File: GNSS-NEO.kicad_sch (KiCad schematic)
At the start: 28 parts, among them J3 Conn_Coaxial, J4 Conn_Coaxial_Small, SW1 SW_Push, SW2 SW_Push, U2 NEO-M9N

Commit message: next revision pcb progress
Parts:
- removed D7: BESDU0603-14, Diode_SMD:D_0603_1608Metric, symbol Device:D_TVS
- removed TP1: LNA_EN, TestPoint:TestPoint_Loop_D1.80mm_Drill1.0mm_Beaded, symbol Connector:TestPoint_Probe
- added C28: 100nF, Capacitor_SMD:C_0402_1005Metric, symbol Device:C_Small
- added C30: 10uF, Capacitor_SMD:C_0402_1005Metric, symbol Device:C_Small
- added C31: 47pF C0G/NP0, Capacitor_SMD:C_0402_1005Metric, symbol Device:C_Small
- added C32: 10uF, Capacitor_SMD:C_0603_1608Metric, symbol Device:C_Small
- added C33: 22pF C0G/NP0, Capacitor_SMD:C_0402_1005Metric, symbol Device:C_Small
- added C34, C35: 10nF, Capacitor_SMD:C_0402_1005Metric_Pad0.74x0.62mm_HandSolder, symbol Device:C_Small
- added D1: TI ESD501, Package_SON:Texas_DPY0002A_0.6x1mm_P0.65mm, symbol Device:D_TVS
- added D8: ESD501, Package_SON:Texas_DPY0002A_0.6x1mm_P0.65mm, symbol Device:D_TVS
- added FB2: BLM18HG601SN1D, Inductor_SMD:L_0603_1608Metric, symbol Device:FerriteBead
- added FL1: B39162B4327P810, Filter:Filter_1411-5_1.4x1.1mm, symbol Filter:SF14-1575F5UUC1
- added JP4: SolderJumper_3_Bridged12, Jumper:SolderJumper-3_P1.3mm_Bridged12_RoundedPad1.0x1.5mm_NumberLabels, symbol Jumper:SolderJumper_3_Bridged12
- added Q2: AO3401A, Package_TO_SOT_SMD:SOT-23, symbol Transistor_FET:AO3401A
- added Q5: BSS138, Package_TO_SOT_SMD:SOT-23, symbol Transistor_FET:BSS138
- added R30, R34: 100k, symbol Device:R_Small
- added R31: 1k, symbol Device:R_Small
- added R32: 0, Resistor_SMD:R_0402_1005Metric_Pad0.72x0.64mm_HandSolder, symbol Device:R
- added R33: 68, Resistor_SMD:R_0402_1005Metric_Pad0.72x0.64mm_HandSolder, symbol Device:R
- added R35, R36: 100, Resistor_SMD:R_0402_1005Metric_Pad0.72x0.64mm_HandSolder, symbol Device:R
- added U8: TPS259573DSGR, easyeda2kicad:WSON-8_L2.0-W2.0-P0.50-TL-EP, symbol easyeda2kicad:TPS259573DSGR
- C10: value 100nF -> 1uF XR7
- L1: value 22nH -> 47nH; LCSC Part C6364694 -> C98077
- R13: value 10 -> 68 ohm >=500mW; footprint Resistor_SMD:R_0402_1005Metric -> Resistor_SMD:R_1206_3216Metric_Pad1.30x1.75mm_HandSolder
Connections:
- net +3V3: now also C28.1
- net GND: now also C28.2, C30.2, C32.1, C33.2, C34.2, C35.2, D1.1 (A1), D8.2 (A2), FL1.2, FL1.3, FL1.5, Q5.2 (S), R34.2, R35.1, R36.1
- net GPS_ANT: now also R33.2, R35.2; no longer L1.1, R27.2, R28.2
- net VCC_RF: now also JP4.3 (B); no longer R13.2
- net LNA_EN: now reaches U2.14 (LNA_EN)
- net LNA_EN: now also R31.2
- net at C10.1, L1.2, R13.1: now also C33.1
- net AFT_GPS_ANT: no longer names the net of J3.1 (In), R28.1
- net AFT_GPS_ANT: now also D1.2 (A2)
- new net: C30.1, C32.2, FB2.1, Q2.2 (S), R30.1
- new net: C35.1, FL1.1, R32.2
- new net: FB2.2, JP4.2 (C)
- new net: C31.1, C34.1, R32.1
- new net: C31.2, D8.1 (A1), L1.1, R27.2, R28.2
- new net: FL1.4, R33.1, R36.2
- new net: Q5.1 (G), R31.1, R34.1
- new net: Q2.1 (G), Q5.3 (D), R30.2
- new net: Q2.3 (D), R13.2
- new net +5V: JP4.1 (A)
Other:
- note added: "Active Antenna only"
- note added: "Antenna only powered when module is not in sleep mode"
- note added: "Attenuate 10dB"
- note added: "Bandpass GNSS SAW filter"
- note added: "Current limiting"
- note added: "If using VCC_RF, drop to 10 ohms"
- note added: "Optional Matching"
- note added: "maybe: replace with TPS2553"
- moved on the sheet: C10, D2, D3, J3, J4, JP1, JP2, JP3, JP5, L1, R10, R11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

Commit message: update schematic with new eFuse and add journal.md
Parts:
- removed U8: TPS259573DSGR, easyeda2kicad:WSON-8_L2.0-W2.0-P0.50-TL-EP, symbol easyeda2kicad:TPS259573DSGR
- added BT3: Battery_Cell, symbol Device:Battery_Cell
- added C39: 10uF, Capacitor_SMD:C_0402_1005Metric, symbol Device:C_Small
- added C40: 2.2nF, symbol Device:C_Small
- added C41: 1uF, Capacitor_SMD:C_0402_1005Metric, symbol Device:C_Small
- added C42: 3.3nF, symbol Device:C_Small
- added JP7: DISABLE_PROT, symbol Jumper:SolderJumper_2_Open
- added R29: 200k, symbol Device:R_Small
- added R38, R39: 100k, symbol Device:R_Small
- added R41: 10k, symbol Device:R_Small
- added R42: 6.65k, symbol Device:R_Small
- added R43: 47k, symbol Device:R_Small
- added U5: TPS259470LRPWR, easyeda2kicad:VQFN-10_L2.0-W2.0-P0.45-TL, symbol easyeda2kicad:TPS259470LRPWR
- C28: value 100nF -> 10uF
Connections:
- net +3V3: now also C41.2, JP7.1 (A), R29.1, R39.1, R41.1, R43.1, U5.5 (IN); no longer C16.1, C17.1, C28.1, JP1.1 (A), R8.1, U2.22 (V_BCKP), U2.23 (VCC)
- net GND: now also BT3.2 (-), C39.2, C40.1, C41.1, C42.2, R38.2, R42.2, U5.8 (GND)
- new net: BT3.1 (+), U2.22 (V_BCKP)
- new net: R41.2, U5.1 (EN/UVLO)
- new net: C40.2, U5.10 (ITIMER)
- new net: R29.2, R38.1, U5.2 (OVLO/OVCSEL)
- new net: R43.2, U5.3 (PG/AUXOFF)
- new net: C42.1, U5.7 (DVDT)
- new net: R42.1, U5.9 (ILM)
- new net 3V3_GNSS: C16.1, C17.1, C28.1, C39.1, JP1.1 (A), JP7.2 (B), R8.1, U2.23 (VCC), U5.6 (OUT)
- new net FLT_GNSS: R39.2, U5.4 (~{FLT}/PGTH)
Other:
- moved on the sheet: R14, R7, SW1, SW2, TP2, U2

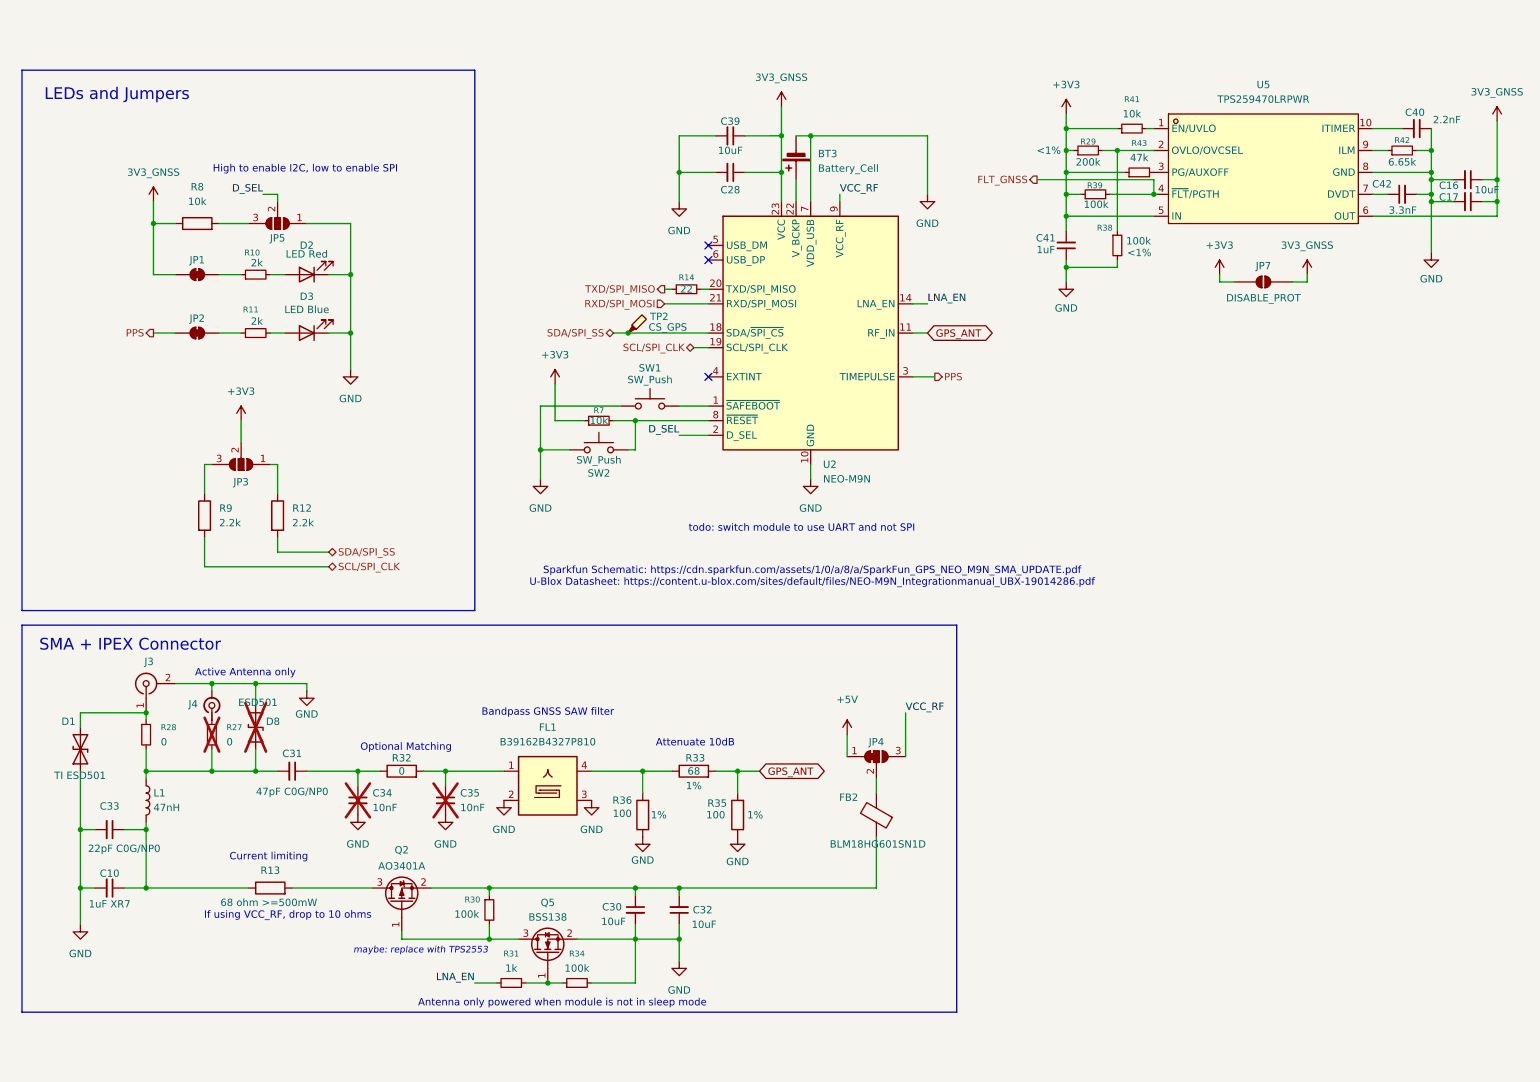
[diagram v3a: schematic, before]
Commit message: revise efuse, add bat
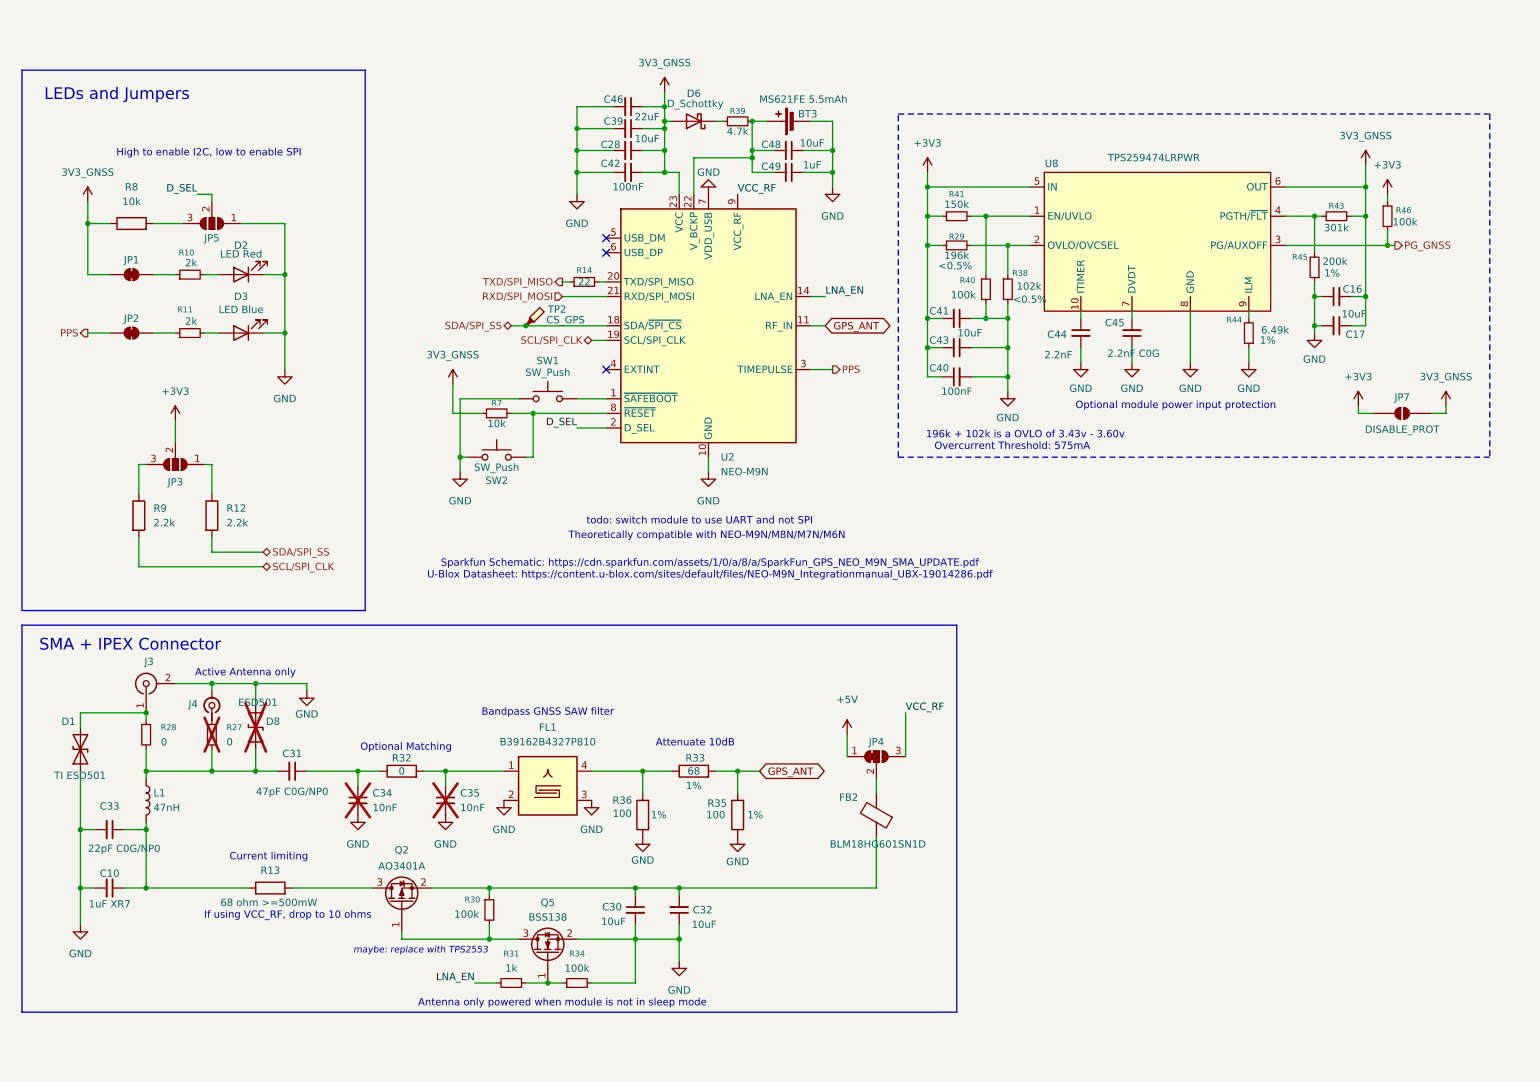
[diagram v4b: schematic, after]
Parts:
- removed R42: 6.65k, symbol Device:R_Small
- removed U5: TPS259470LRPWR, easyeda2kicad:VQFN-10_L2.0-W2.0-P0.45-TL, symbol easyeda2kicad:TPS259470LRPWR
- added C43, C48: 10uF, Capacitor_SMD:C_0402_1005Metric, symbol Device:C_Small
- added C44: 2.2nF, symbol Device:C_Small
- added C45: 2.2nF C0G, Capacitor_SMD:C_0402_1005Metric, symbol Device:C_Small
- added C46: 22uF, Capacitor_SMD:C_0805_2012Metric, symbol Device:C_Small
- added C49: 1uF, Capacitor_SMD:C_0402_1005Metric, symbol Device:C_Small
- added D6: D_Schottky, symbol Device:D_Schottky
- added R40, R46: 100k, symbol Device:R_Small
- added R44: 6.49k, Resistor_SMD:R_0603_1608Metric_Pad0.98x0.95mm_HandSolder, symbol Device:R_Small
- added R45: 200k, Resistor_SMD:R_0603_1608Metric_Pad0.98x0.95mm_HandSolder, symbol Device:R_Small
- added U8: TPS259474LRPWR, easyeda2kicad:VQFN-10_L2.0-W2.0-P0.45-TL, symbol easyeda2kicad:TPS259474LRPWR
- BT3: value Battery_Cell -> MS621FE 5.5mAh; footprint (none) -> Battery:BatteryHolder_Seiko_MS621F; now left out of the parts list
- C16, C39: footprint Capacitor_SMD:C_0402_1005Metric -> Capacitor_SMD:C_0603_1608Metric
- C40: value 2.2nF -> 100nF; footprint (none) -> Capacitor_SMD:C_0402_1005Metric
- C41: value 1uF -> 10uF; footprint Capacitor_SMD:C_0402_1005Metric -> Capacitor_SMD:C_0603_1608Metric
- C42: value 3.3nF -> 100nF; footprint (none) -> Capacitor_SMD:C_0402_1005Metric
- R29: value 200k -> 196k; footprint (none) -> Resistor_SMD:R_0603_1608Metric_Pad0.98x0.95mm_HandSolder; Tolerance <1% -> <0.5%
- R38: value 100k -> 102k; footprint (none) -> Resistor_SMD:R_0603_1608Metric_Pad0.98x0.95mm_HandSolder; Tolerance <1% -> <0.5%
- R39: value 100k -> 4.7k; footprint (none) -> Resistor_SMD:R_0402_1005Metric
- R41: value 10k -> 150k
- R43: value 47k -> 301k
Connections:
- net FLT_GNSS is gone; now on an unnamed net: R39.2
- net +3V3: now also C40.1, C43.2, R46.1, U8.5 (IN); no longer R39.1, R43.1, R7.1
- net 3V3_GNSS: now also C16.2, C42.2, R43.2, R7.1, C46.1, D6.2 (A), U8.6 (OUT); no longer C16.1
- net GND: now also C16.1, C40.2, C42.1, C43.1, C44.2, C45.1, C46.2, C48.1, C49.1, R40.2, R44.1, R45.1, U8.8 (GND); no longer C16.2, C40.1, C42.2
- net at BT3.1 (+), U2.22 (V_BCKP): now also C48.2, C49.2
- net at R41.2: now also R40.1, U8.1 (EN/UVLO)
- net at R29.2, R38.1: now also U8.2 (OVLO/OVCSEL)
- new net: R43.1, R45.2, U8.4 (PGTH/~{FLT})
- new net: D6.1 (K), R39.1
- new net: C44.1, U8.10 (ITIMER)
- new net: R44.2, U8.9 (ILM)
- new net: C45.2, U8.7 (DVDT)
- new net PG_GNSS: R46.2, U8.3 (PG/AUXOFF)
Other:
- note added: "196k + 102k is a OVLO of 3.43v - 3.60v"
- note added: "Optional module power input protection"
- note added: "Overcurrent Threshold: 575mA"
- note added: "Theoretically compatible with NEO-M9N/M8N/M7N/M6N"
- moved on the sheet: C28, C39, D2, D3, JP1, JP2, JP3, JP5, R10, R11, R12, R14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

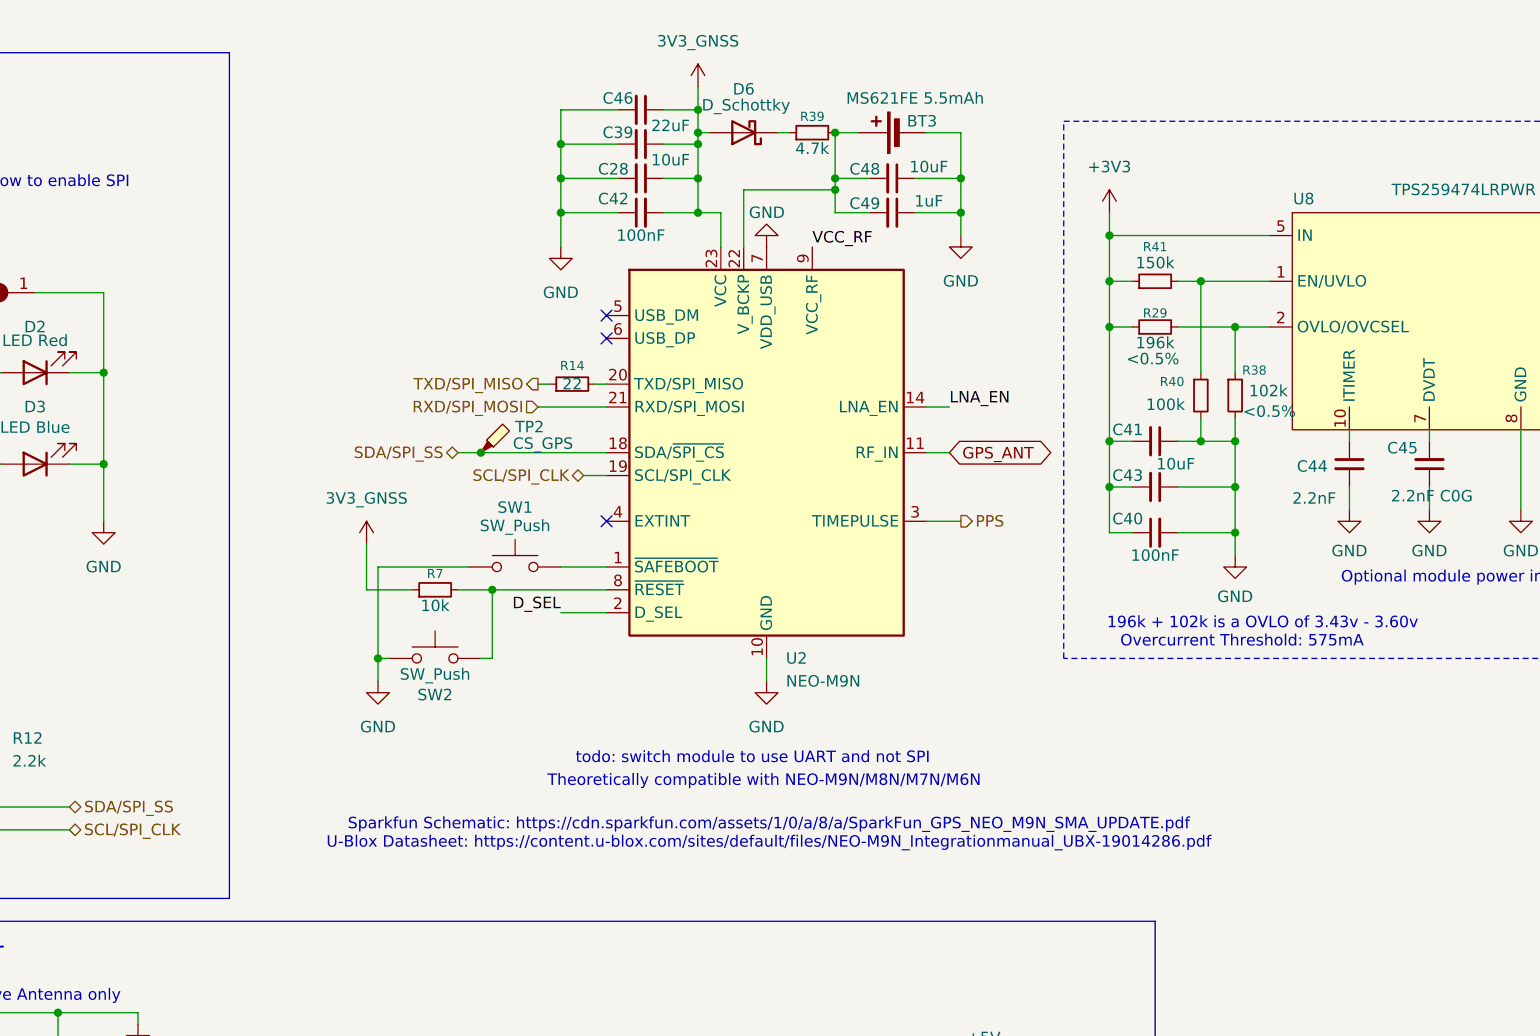
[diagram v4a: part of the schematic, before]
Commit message: add BMS and charge controller!
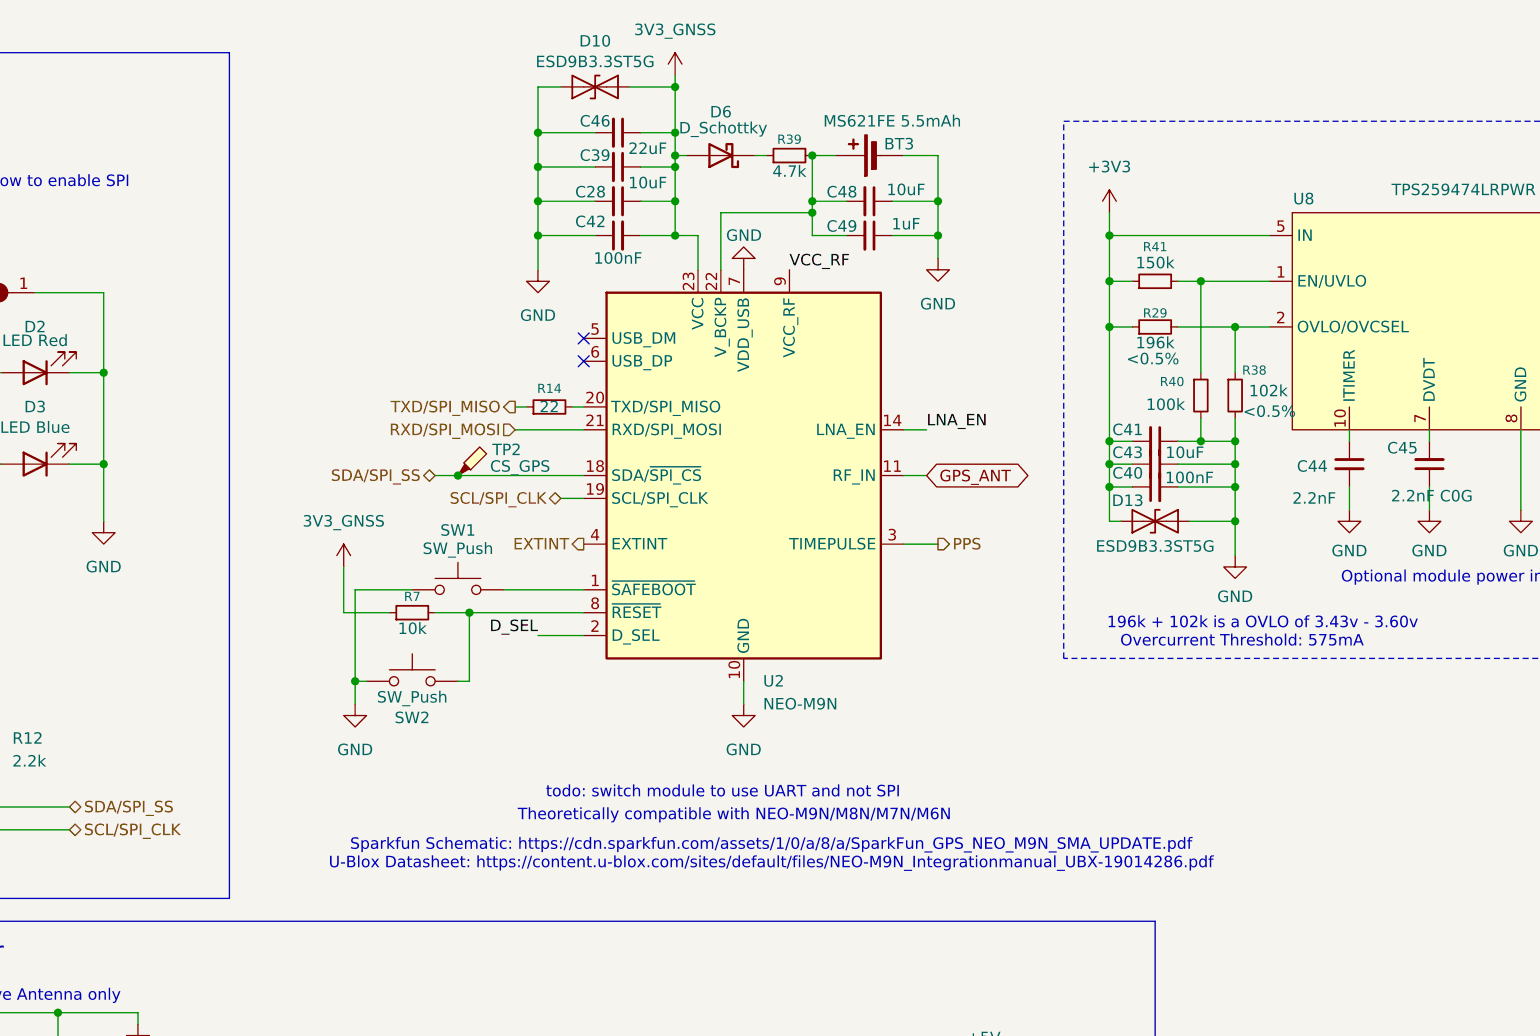
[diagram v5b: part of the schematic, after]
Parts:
- added D10, D13: ESD9B3.3ST5G, Diode_SMD:D_SOD-923, symbol Diode:ESD9B3.3ST5G
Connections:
- net +3V3: now also D13.1 (A1)
- net 3V3_GNSS: now also D10.2 (A2)
- net GND: now also D10.1 (A1), D13.2 (A2)
- net EXTINT: now reaches U2.4 (EXTINT)
- no-connect marks 3 -> 2
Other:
- moved on the sheet: BT3, C28, C39, C40, C42, C43, C46, C48, C49, D6, R14, R39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
